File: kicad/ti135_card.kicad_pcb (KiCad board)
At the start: 8 copper layers, 76 x 65.1 mm, 293 parts, among them J1 JTAG 3.3V, J2 UART 3.3V, J3 2x19 1.27mm socket (bottom), J5 LCD 1x14 2.54mm, J6 2x3 1.27mm (bottom), J9 HR911130A, U1001 THGAMVG7T13BAIL, U101 NCP163ASN330T1G, U1201 SN74AXC8T245PWR, U1202 SN74AXC8T245PWR, U1203 SN74AXC8T245PWR, U1204 SN74AXC8T245PWR, U1301 SN74LV4051APWR, U1302 OPA365AIDBVR, U1303 ADS7056IRUGR, U201 TLV62585PDRLR, U301 TLV62585PDRLR, U311 TLV62585PDRLR, U331 TLV62585PDRLR, U341 TLV62585PDRLR, U401 TPS3808G01DBVR, U501 Ti135N484I3, U601 IS25WP128-RHLE, U801 H9HCNNN8KUMLHR-NME, U901 RTL8211FDI-CG, U902 74LVC1G07GW, Y701 SiT8924BA-73-18N-25.000000, Y901 25MHz

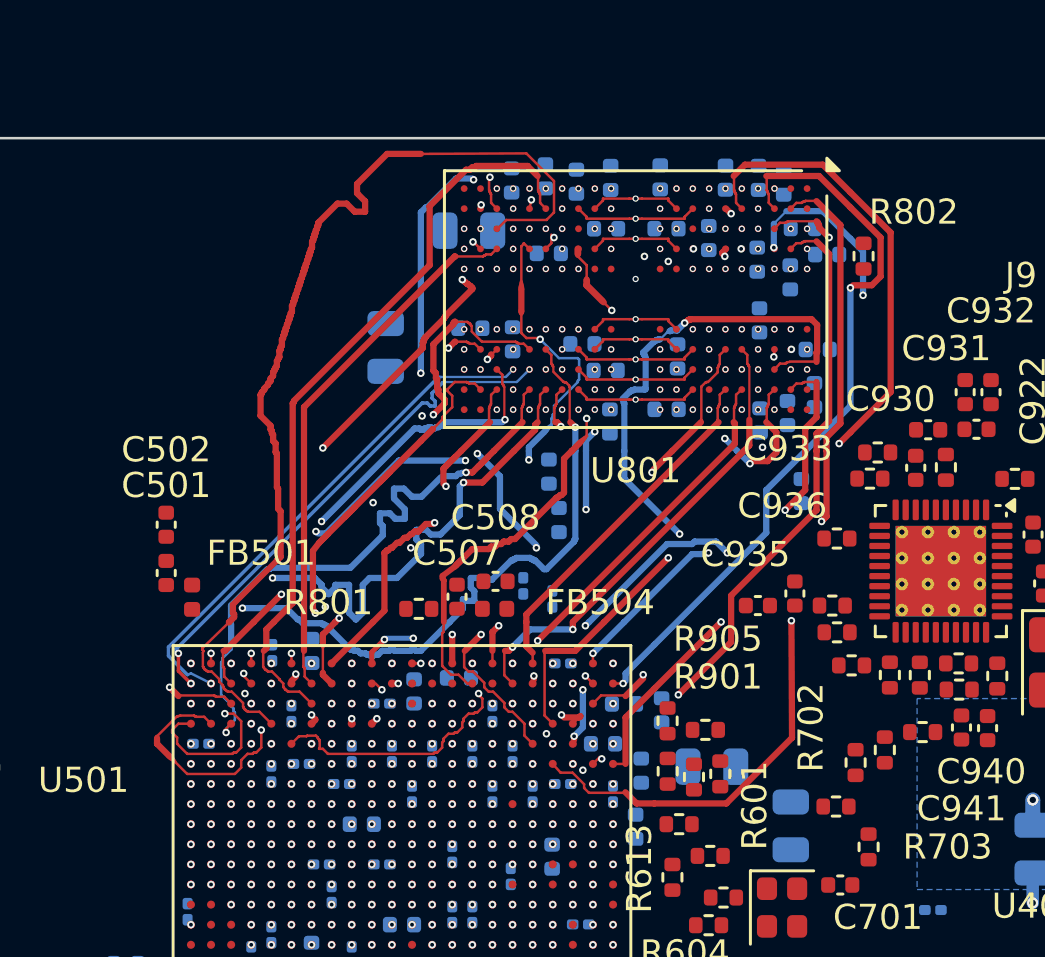
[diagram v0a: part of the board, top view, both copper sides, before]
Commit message: Phase 1: LPDDR4 from ddr-option2 transplanted onto main
tools/ddr/transplant.py swaps the ddr_* copper; C528 moved 0.3 mm off a dq2 via.
DQ-DQS -23.9..+60.4 ps, CK-DQS <= 86 ps, CA-CK -57.1..+47.0 ps (die to die); parity 0,
non-DDR DRC unchanged; 88 mm below the DDR width minimum (phase 2).

Co-Authored-By: Claude Opus 5.5 <noreply@anthropic.com>
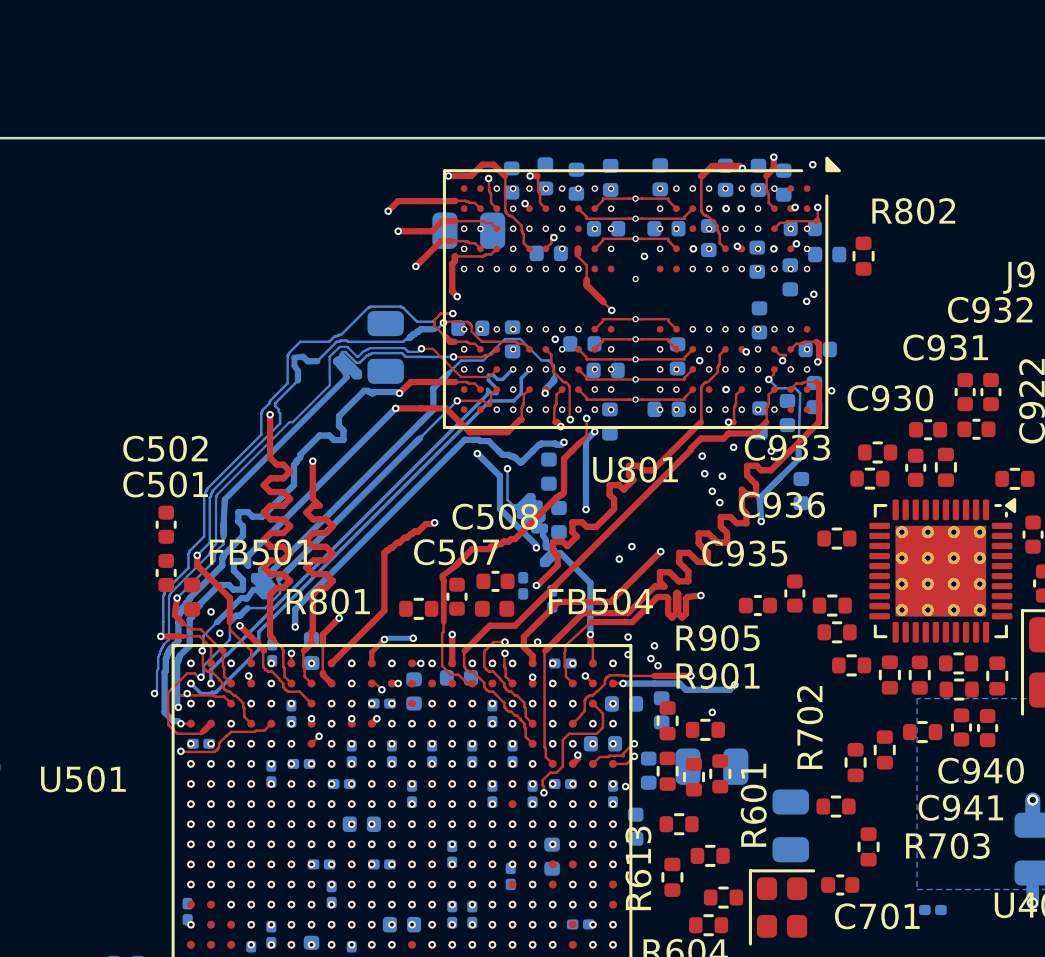
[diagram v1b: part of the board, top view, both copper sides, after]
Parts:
- moved C528 0.30 mm to (173.8, 76.9)
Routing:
- net /08 lpddr4/ddr_dq4: track 25.8 -> 43.5 mm
- net /08 lpddr4/ddr_dq13: track 14.3 -> 27.3 mm, vias 0 -> 4
- net /08 lpddr4/ddr_dq3: track 28.9 -> 41.7 mm
- net /08 lpddr4/ddr_dq6: track 25.7 -> 37.6 mm
- net /08 lpddr4/ddr_dq1: track 27.3 -> 39.1 mm
- net /08 lpddr4/ddr_dq2: track 28.0 -> 37.7 mm
- net /08 lpddr4/ddr_dq21: track 41.8 -> 32.4 mm, vias 3 -> 2
- net /08 lpddr4/ddr_dq12: track 15.0 -> 23.1 mm, vias 2 -> 3
- net /08 lpddr4/ddr_dq16: track 21.4 -> 28.7 mm, vias 0 -> 2
- net /08 lpddr4/ddr_dm2: track 40.4 -> 33.6 mm, vias 0 -> 2
- net /08 lpddr4/ddr_dq5: track 29.6 -> 35.9 mm, vias 2 -> 3
- net /08 lpddr4/ddr_dq25: track 21.0 -> 27.0 mm, vias 3 -> 2
- net /08 lpddr4/ddr_dm1: track 28.5 -> 22.5 mm
- net /08 lpddr4/ddr_dq18: track 35.3 -> 29.3 mm, vias 7 -> 2
- net /08 lpddr4/ddr_dq22: track 38.1 -> 32.7 mm, vias 4 -> 3
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
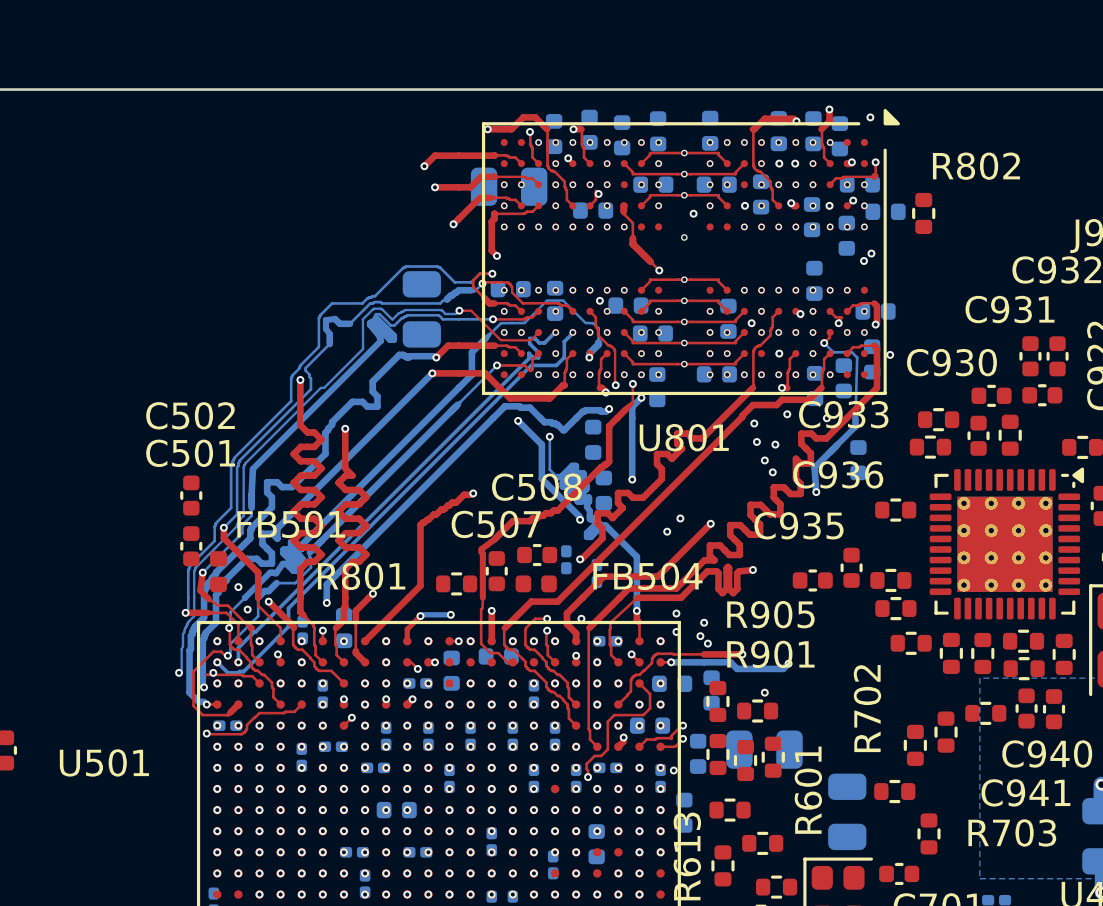
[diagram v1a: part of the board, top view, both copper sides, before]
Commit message: Phase 2: LPDDR4 at the 40 ohm width everywhere, timing within the checklist
Re-routed the ten narrow DDR nets at width (reroute_nets.sh, --escalation off),
meandered dm0/dq1, re-routed DQS0 as a pair. 0 mm below the width minimum, no
track_width errors; DQ/DM-DQS, CK-DQS and CA-CK within decision 1 by both the path
model and KiCad's readout. DQS P/N 0.53/6.64/0.07/5.61 ps, CK 3.67 ps. Bytes 0 and 3
less on one layer (B.Cu has no room at 0.25 mm). Rest of the board unchanged.

Co-Authored-By: Claude Opus 5.5 <noreply@anthropic.com>
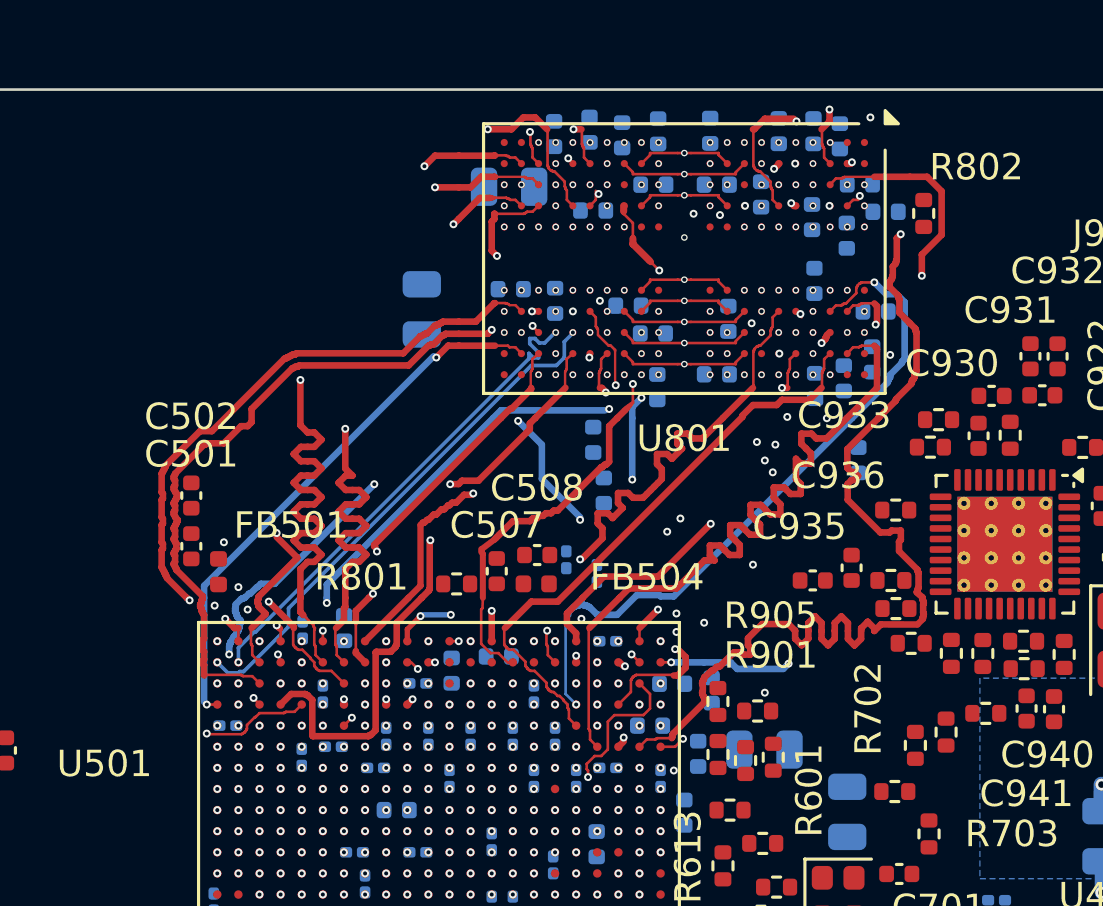
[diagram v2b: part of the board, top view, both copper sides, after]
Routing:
- net /08 lpddr4/ddr_dq26: track 26.1 -> 20.0 mm
- net /08 lpddr4/ddr_dq31: track 26.5 -> 22.0 mm, vias 3 -> 4
- net /08 lpddr4/ddr_dm1: track 22.5 -> 18.4 mm
- net /08 lpddr4/ddr_dq6: track 37.6 -> 34.2 mm
- net /08 lpddr4/ddr_dq28: track 24.1 -> 20.7 mm
- net /08 lpddr4/ddr_dq30: track 28.5 -> 25.2 mm
- net /08 lpddr4/ddr_dq10: track 23.6 -> 26.8 mm, vias 4 -> 2
- net /08 lpddr4/ddr_dq25: track 27.0 -> 24.8 mm
- net /08 lpddr4/ddr_dm0: track 38.7 -> 36.5 mm, vias 2 -> 3
- net /08 lpddr4/ddr_dq1: track 39.1 -> 40.2 mm
- net /08 lpddr4/ddr_dq27: track 27.5 -> 26.7 mm
- net /08 lpddr4/ddr_dqs0_P: track 33.2 -> 34.0 mm, vias 4 -> 2
- net /08 lpddr4/ddr_dq24: track 25.6 -> 25.9 mm, vias 2 -> 4
- net /08 lpddr4/ddr_dqs0_N: track 34.2 -> 33.9 mm, vias 4 -> 2
- net /08 lpddr4/ddr_dm3: vias 3 -> 2
